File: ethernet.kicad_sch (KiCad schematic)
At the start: 17 parts, among them J3 HR911130C, U1 AM6254ATCGHAALW, U6 RTL8211F-CG

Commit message: Ethernet chip wiring
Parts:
- added R65: RC0402FR-072K49L, pepy_sym_lib:[RES_SMD_0402_1005Metric], symbol pepy_sym_lib:[RES_SMD_0402_1005Metric]YAGEO RC0402FR-072K49L
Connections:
- net GND: now also R65.2
- net at U6.39 (RSET): now also R65.1
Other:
- note added: "Place resistors close to IC"
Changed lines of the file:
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@@
 	(generator_version "9.0")
 	(paper "A3")
+	(text "Place resistors close to IC\n"
+		(exclude_from_sim no)
+		(at 133.096 259.588 0)
+		(effects
+			(font
+				(size 1.27 1.27)
+			)
+		)
+	)
 	(text "2kV Cap\n"
 		(exclude_from_sim no)
@@
 	)
 	(symbol
+		(lib_id "power:GND")
+		(at 120.65 85.09 90)
+		(unit 1)
+		(exclude_from_sim no)
+		(in_bom yes)
+		(on_board yes)
+		(dnp no)
+		(property "Reference" "#PWR037"
+			(at 127 85.09 0)
+			(effects
+				(font
+					(size 1.27 1.27)
+				)
+				(hide yes)
+			)
+		)
+		(property "Value" "GND"
+			(at 123.698 85.09 90)
+			(effects
+				(font
+					(size 1.27 1.27)
+				)
+				(justify right)
+			)
+		)
+		(property "Footprint" ""
+			(at 120.65 85.09 0)
+			(effects
+				(font
+					(size 1.27 1.27)
+				)
+				(hide yes)
+			)
+		)
+		(property "Datasheet" ""
+			(at 120.65 85.09 0)
+			(effects
+				(font
+					(size 1.27 1.27)
+				)
+				(hide yes)
+			)
+		)
+		(property "Description" "Power symbol creates a global label with name \"GND\" , ground"
+			(at 120.65 85.09 0)
+			(effects
+				(font
+					(size 1.27 1.27)
+				)
+				(hide yes)
+			)
+		)
+		(pin "1"
+		)
+		(instances
+			(project ""
+				(path "/30d6913c-7aa4-4f56-9882-2ba08f7e2cce/0115f286-8e80-4bc6-a636-ca28db07176d"
+					(reference "#PWR037")
+					(unit 1)
+				)
+			)
+		)
+	)
+	(symbol
 		(lib_id "pepy_sym_lib:[RES_SMD_0201_0603Metric]YAGEO RC0201FR-0733RL")
 		(at 93.98 242.57 0)
@@
 					(unit 1)
 				)
+			)
+		)
+	)
+	(symbol
+		(lib_id "pepy_sym_lib:[RES_SMD_0402_1005Metric]YAGEO RC0402FR-072K49L")
+		(at 115.57 85.09 0)
+		(unit 1)
+		(exclude_from_sim no)
+		(in_bom yes)
+		(on_board yes)
+		(dnp no)
+		(property "Reference" "R65"
+			(at 115.57 81.28 0)
+			(effects
+				(font
+					(size 1.27 1.27)
+				)
+			)
+		)
+		(property "Value" "RC0402FR-072K49L"
+			(at 115.57 90.17 0)
+			(effects
+				(font
+					(size 1.27 1.27)
+				)
+				(hide yes)
+			)
+		)
+		(property "Footprint" "pepy_sym_lib:[RES_SMD_0402_1005Metric]"
+			(at 115.57 92.71 0)
+			(effects
+				(font
+					(size 1.27 1.27)
+				)
+				(hide yes)
+			)
+		)
+		(property "Datasheet" "https://www.lcsc.com/product-detail/Chip-Resistor-Surface-Mount_YAGEO-RC0402FR-072K49L_C145071.html"
+			(at 115.57 95.25 0)
+			(effects
+				(font
+					(size 1.27 1.27)
+				)
+				(hide yes)
+			)
+		)
+		(property "Description" "1/16W Thick Film Resistors 50V ±100ppm/℃ ±1% 2.49kΩ 0402 Chip Resistor - Surface Mount ROHS"
+			(at 115.062 100.33 0)
+			(effects
+				(font
+					(size 1.27 1.27)
+				)
+				(hide yes)
+			)
+		)
+		(property "LCSC Part" "C145071"
+			(at 115.57 97.79 0)
+			(effects
+				(font
+					(size 1.27 1.27)
+				)
+				(hide yes)
+			)
+		)
+		(property "Nvalue" "2.49k"
+			(at 115.57 83.058 0)
+			(effects
+				(font
+					(size 1.27 1.27)
+				)
+			)
+		)
+		(property "Manufacturer" "YAGEO"
+			(at 114.554 102.616 0)
+			(effects
+				(font
+					(size 1.27 1.27)
+				)
+				(hide yes)
+			)
+		)
+		(property "Package" "0402"
+			(at 115.316 104.648 0)
+			(effects
+				(font
+					(size 1.27 1.27)
+				)
+				(hide yes)
+			)
+		)
+		(pin "2"
+		)
+		(pin "1"
+		)
+		(instances
+			(project ""
+				(path "/30d6913c-7aa4-4f56-9882-2ba08f7e2cce/0115f286-8e80-4bc6-a636-ca28db07176d"
+					(reference "R65")
+					(unit 1)
+				)

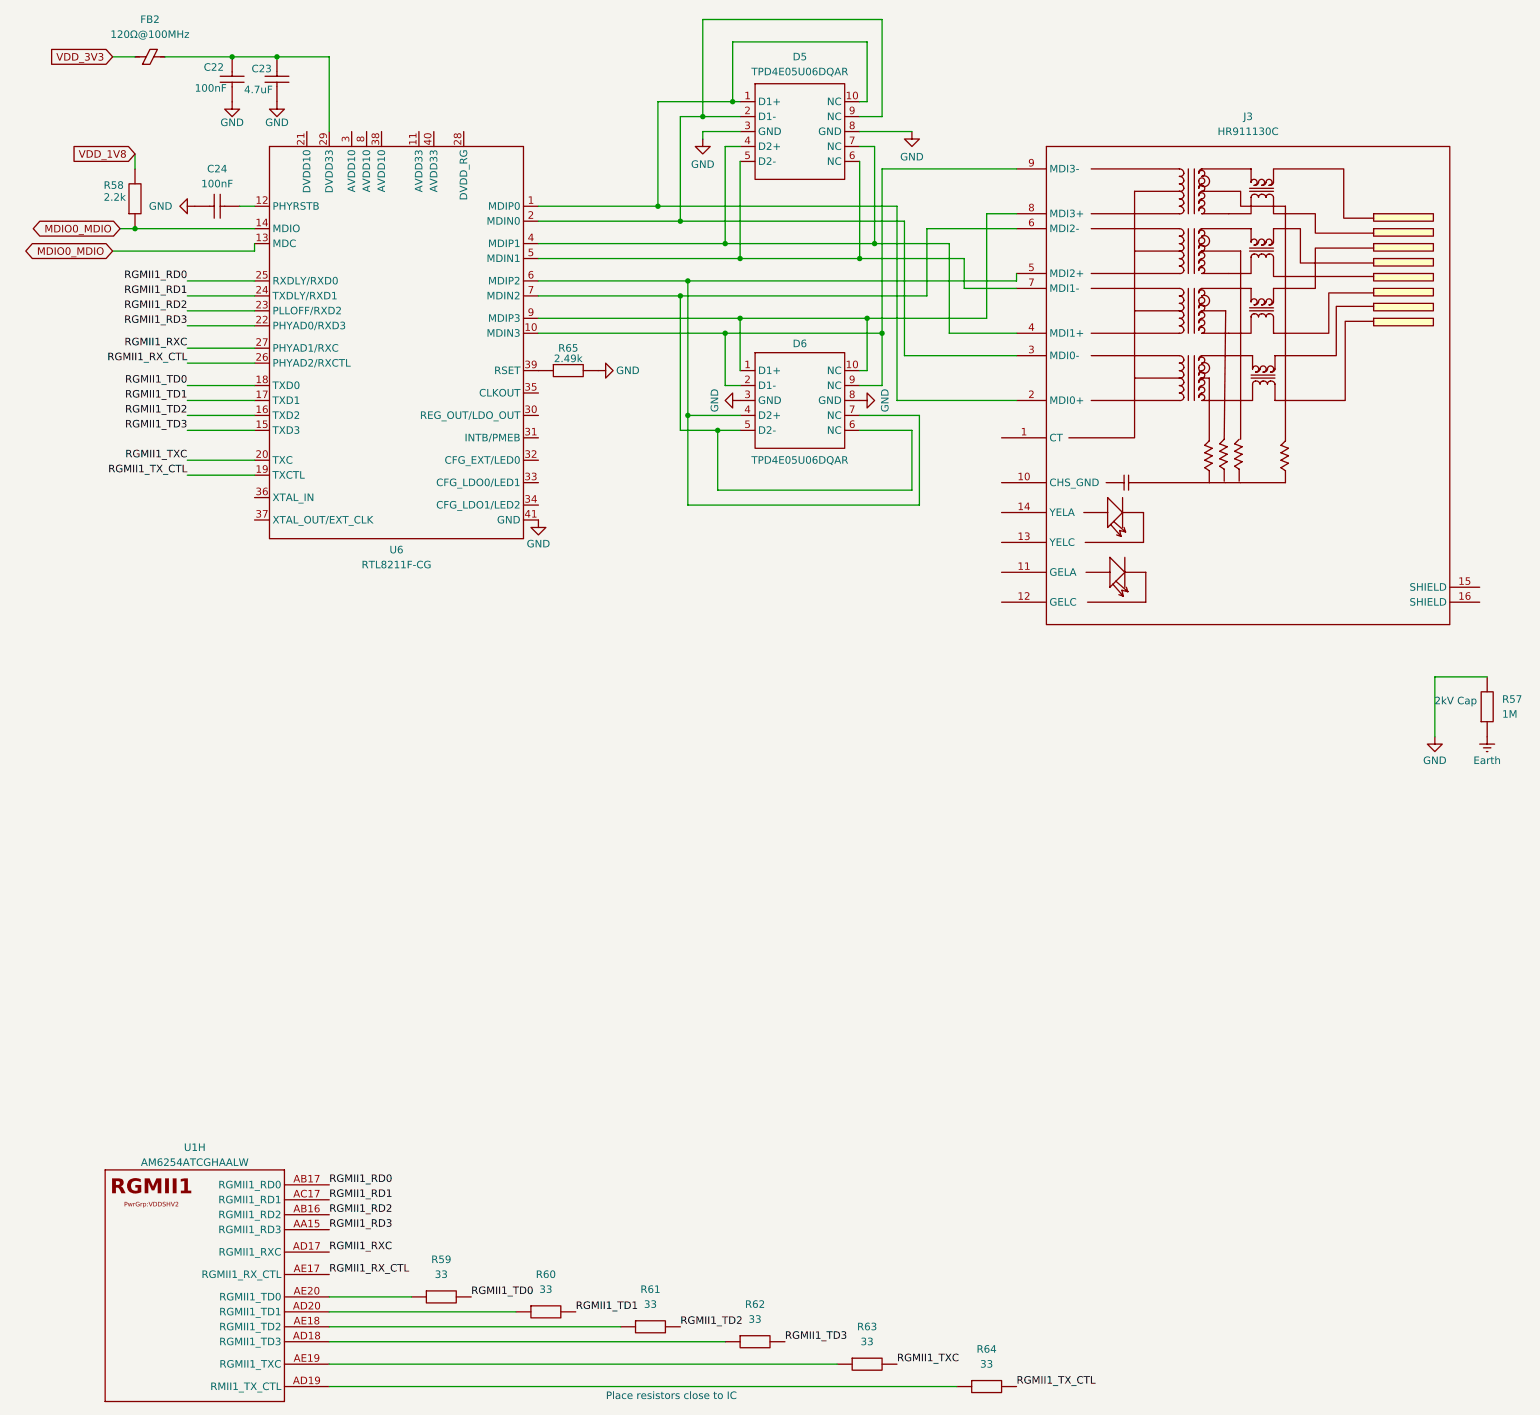
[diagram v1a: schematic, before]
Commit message: SD card changes
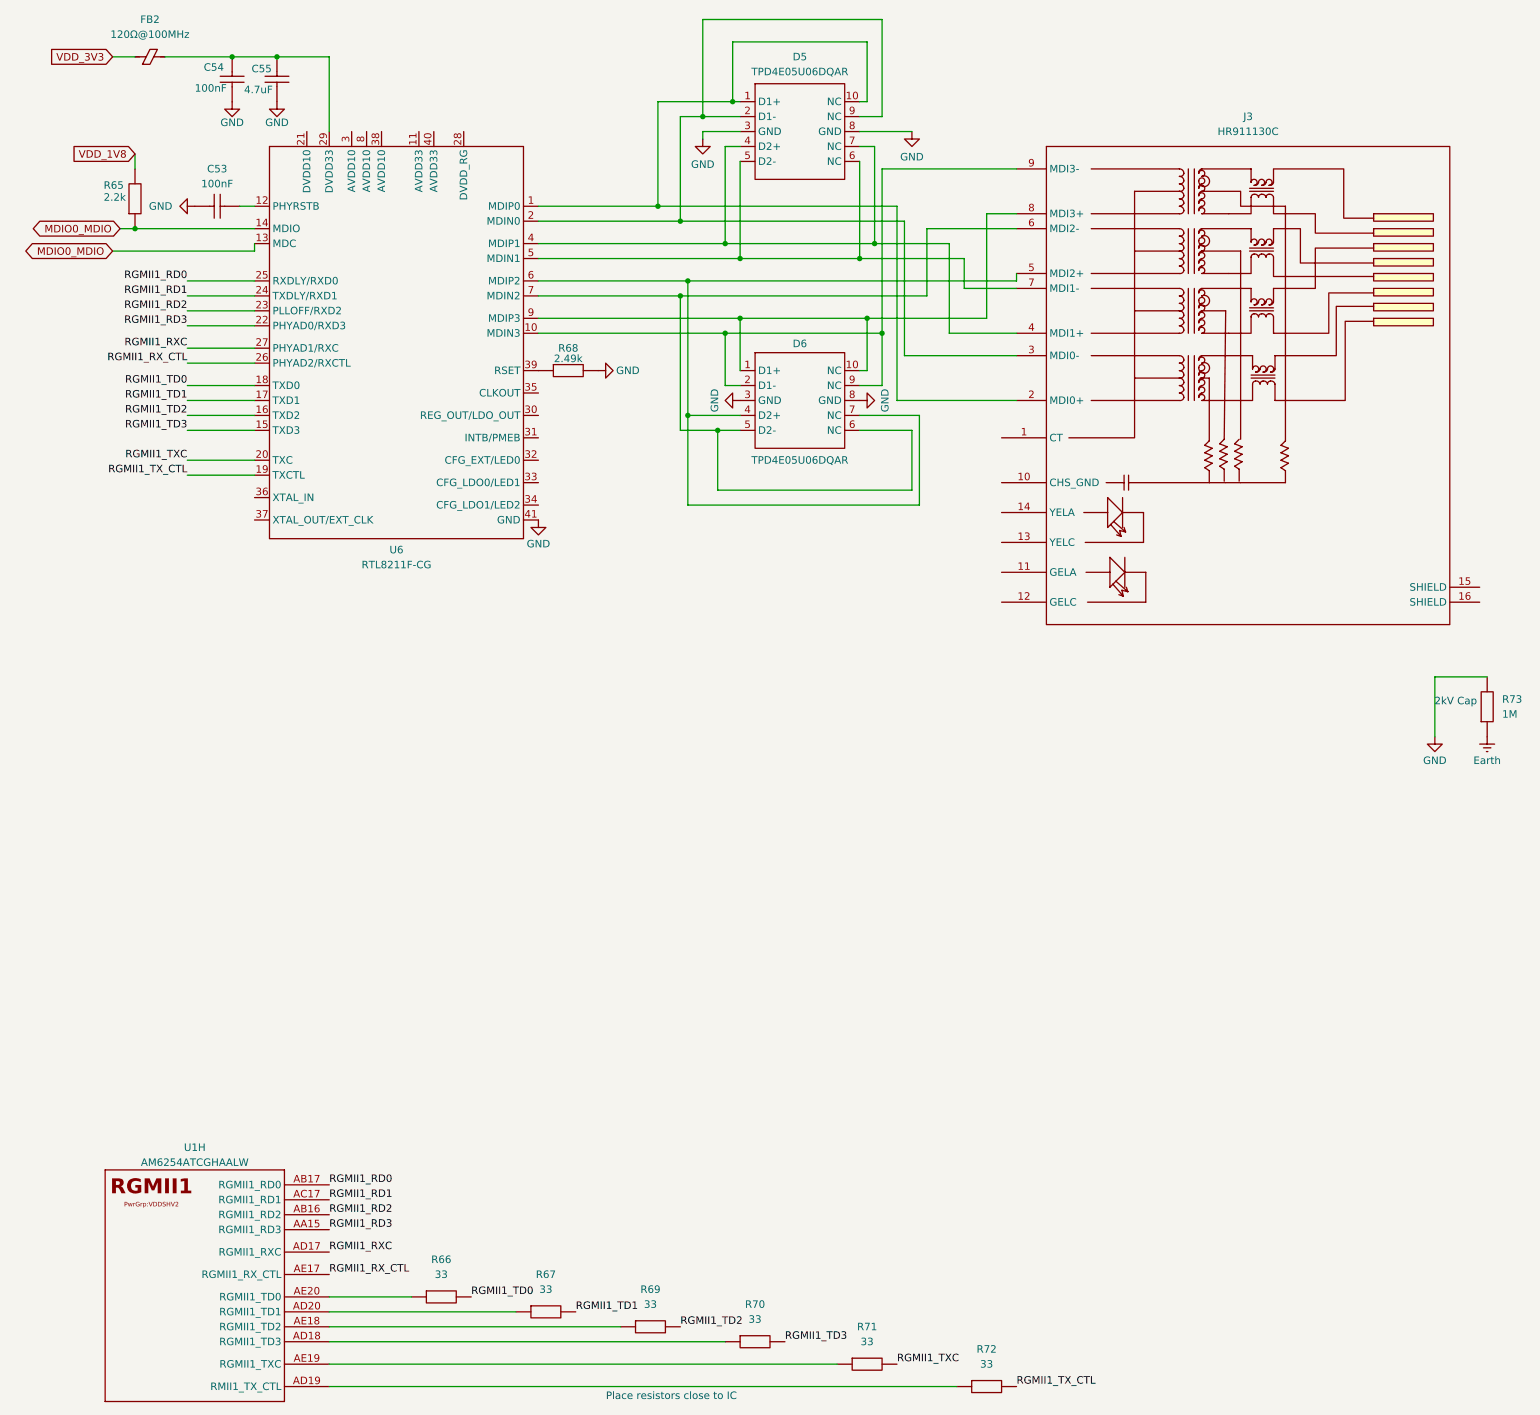
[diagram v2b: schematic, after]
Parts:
- renumbered C24 to C53, C22 to C54, C23 to C55, R58 to R65, R59 to R66, R60 to R67, R65 to R68, R61 to R69, R62 to R70, R63 to R71, R64 to R72, R57 to R73
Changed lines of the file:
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@@
 		(on_board yes)
 		(dnp no)
-		(property "Reference" "#PWR035"
+		(property "Reference" "#PWR050"
 			(at 171.45 90.17 0)
 			(effects
@@
 			(project "dashcam"
 				(path "/30d6913c-7aa4-4f56-9882-2ba08f7e2cce/0115f286-8e80-4bc6-a636-ca28db07176d"
-					(reference "#PWR035")
+					(reference "#PWR050")
 					(unit 1)
 				)
@@
 		(on_board yes)
 		(dnp no)
-		(property "Reference" "#PWR030"
+		(property "Reference" "#PWR053"
 			(at 271.78 153.67 0)
 			(effects
@@
 			(project ""
 				(path "/30d6913c-7aa4-4f56-9882-2ba08f7e2cce/0115f286-8e80-4bc6-a636-ca28db07176d"
-					(reference "#PWR030")
+					(reference "#PWR053")
 					(unit 1)
 				)
@@
 		(dnp no)
 		(fields_autoplaced yes)
-		(property "Reference" "R61"
+		(property "Reference" "R69"
 			(at 129.54 241.3 0)
 			(effects
@@
 			(project "dashcam"
 				(path "/30d6913c-7aa4-4f56-9882-2ba08f7e2cce/0115f286-8e80-4bc6-a636-ca28db07176d"
-					(reference "R61")
+					(reference "R69")
 					(unit 1)
 				)
@@
 		(dnp no)
 		(fields_autoplaced yes)
-		(property "Reference" "#PWR036"
+		(property "Reference" "#PWR043"
 			(at 45.72 57.15 0)
 			(effects
@@
 			(project ""
 				(path "/30d6913c-7aa4-4f56-9882-2ba08f7e2cce/0115f286-8e80-4bc6-a636-ca28db07176d"
-					(reference "#PWR036")
+					(reference "#PWR043")
 					(unit 1)
 				)
@@
 		(on_board yes)
 		(dnp no)
-		(property "Reference" "#PWR028"
+		(property "Reference" "#PWR044"
 			(at 58.42 45.72 0)
 			(effects
@@
 			(project ""
 				(path "/30d6913c-7aa4-4f56-9882-2ba08f7e2cce/0115f286-8e80-4bc6-a636-ca28db07176d"
-					(reference "#PWR028")
+					(reference "#PWR044")
 					(unit 1)
 				)
@@
 		(on_board yes)
 		(dnp no)
-		(property "Reference" "#PWR031"
+		(property "Reference" "#PWR052"
 			(at 262.89 153.67 0)
 			(effects
@@
 			(project ""
 				(path "/30d6913c-7aa4-4f56-9882-2ba08f7e2cce/0115f286-8e80-4bc6-a636-ca28db07176d"
-					(reference "#PWR031")
+					(reference "#PWR052")
 					(unit 1)
 				)
@@
 		(on_board yes)
 		(dnp no)
-		(property "Reference" "#PWR034"
+		(property "Reference" "#PWR049"
 			(at 138.43 90.17 0)
 			(effects
@@
 			(project "dashcam"
 				(path "/30d6913c-7aa4-4f56-9882-2ba08f7e2cce/0115f286-8e80-4bc6-a636-ca28db07176d"
-					(reference "#PWR034")
+					(reference "#PWR049")
 					(unit 1)
 				)
@@
 		(dnp no)
 		(fields_autoplaced yes)
-		(property "Reference" "R62"
+		(property "Reference" "R70"
 			(at 147.32 243.84 0)
 			(effects
@@
 			(project "dashcam"
 				(path "/30d6913c-7aa4-4f56-9882-2ba08f7e2cce/0115f286-8e80-4bc6-a636-ca28db07176d"
-					(reference "R62")
+					(reference "R70")
 					(unit 1)
 				)
@@
 		(on_board yes)
 		(dnp no)
-		(property "Reference" "#PWR027"
+		(property "Reference" "#PWR046"
 			(at 110.49 116.84 0)
 			(effects
@@
 			(project ""
 				(path "/30d6913c-7aa4-4f56-9882-2ba08f7e2cce/0115f286-8e80-4bc6-a636-ca28db07176d"
-					(reference "#PWR027")
+					(reference "#PWR046")
 					(unit 1)
 				)
@@
 		(on_board yes)
 		(dnp no)
-		(property "Reference" "#PWR029"
+		(property "Reference" "#PWR045"
 			(at 66.04 45.72 0)
 			(effects
@@
 			(project "dashcam"
 				(path "/30d6913c-7aa4-4f56-9882-2ba08f7e2cce/0115f286-8e80-4bc6-a636-ca28db07176d"
-					(reference "#PWR029")
+					(reference "#PWR045")
 					(unit 1)
 				)
@@
 		(on_board yes)
 		(dnp no)
-		(property "Reference" "#PWR037"
+		(property "Reference" "#PWR047"
 			(at 127 85.09 0)
 			(effects
@@
 			(project ""
 				(path "/30d6913c-7aa4-4f56-9882-2ba08f7e2cce/0115f286-8e80-4bc6-a636-ca28db07176d"
-					(reference "#PWR037")
+					(reference "#PWR047")
 					(unit 1)
 				)
@@
 		(dnp no)
 		(fields_autoplaced yes)
-		(property "Reference" "R59"
+		(property "Reference" "R66"
 			(at 93.98 236.22 0)
 			(effects
@@
 			(project ""
 				(path "/30d6913c-7aa4-4f56-9882-2ba08f7e2cce/0115f286-8e80-4bc6-a636-ca28db07176d"
-					(reference "R59")
+					(reference "R66")
 					(unit 1)
 				)
@@
 		(on_board yes)
 		(dnp no)
-		(property "Reference" "#PWR033"
+		(property "Reference" "#PWR048"
 			(at 138.43 52.07 0)
 			(effects
@@
 			(project "dashcam"
 				(path "/30d6913c-7aa4-4f56-9882-2ba08f7e2cce/0115f286-8e80-4bc6-a636-ca28db07176d"
-					(reference "#PWR033")
+					(reference "#PWR048")
 					(unit 1)
 				)
@@
 		(on_board yes)
 		(dnp no)
-		(property "Reference" "R58"
+		(property "Reference" "R65"
 			(at 36.576 53.594 90)
 			(effects
@@
 			(project ""
 				(path "/30d6913c-7aa4-4f56-9882-2ba08f7e2cce/0115f286-8e80-4bc6-a636-ca28db07176d"
-					(reference "R58")
+					(reference "R65")
 					(unit 1)
 				)
@@
 		(dnp no)
 		(fields_autoplaced yes)
-		(property "Reference" "R63"
+		(property "Reference" "R71"
 			(at 166.37 247.65 0)
 			(effects
@@
 			(project "dashcam"
 				(path "/30d6913c-7aa4-4f56-9882-2ba08f7e2cce/0115f286-8e80-4bc6-a636-ca28db07176d"
-					(reference "R63")
+					(reference "R71")
 					(unit 1)
 				)
@@
 		(on_board yes)
 		(dnp no)
-		(property "Reference" "C23"
+		(property "Reference" "C55"
 			(at 61.722 33.782 90)
 			(effects
@@
 			(project ""
 				(path "/30d6913c-7aa4-4f56-9882-2ba08f7e2cce/0115f286-8e80-4bc6-a636-ca28db07176d"
-					(reference "C23")
+					(reference "C55")
 					(unit 1)
 				)
@@
 		(dnp no)
 		(fields_autoplaced yes)
-		(property "Reference" "R64"
+		(property "Reference" "R72"
 			(at 186.69 251.46 0)
 			(effects
@@
 			(project "dashcam"
 				(path "/30d6913c-7aa4-4f56-9882-2ba08f7e2cce/0115f286-8e80-4bc6-a636-ca28db07176d"
-					(reference "R64")
+					(reference "R72")
 					(unit 1)
 				)
@@
 		(dnp no)
 		(fields_autoplaced yes)
-		(property "Reference" "R60"
+		(property "Reference" "R67"
 			(at 111.76 238.76 0)
 			(effects
@@
 			(project "dashcam"
 				(path "/30d6913c-7aa4-4f56-9882-2ba08f7e2cce/0115f286-8e80-4bc6-a636-ca28db07176d"
-					(reference "R60")
+					(reference "R67")
 					(unit 1)
 				)
@@
 		(dnp no)
 		(fields_autoplaced yes)
-		(property "Reference" "C24"
+		(property "Reference" "C53"
 			(at 55.88 50.8 0)
 			(effects
@@
 			(project ""
 				(path "/30d6913c-7aa4-4f56-9882-2ba08f7e2cce/0115f286-8e80-4bc6-a636-ca28db07176d"
-					(reference "C24")
+					(reference "C53")
 					(unit 1)
 				)
@@
 		(on_board yes)
 		(dnp no)
-		(property "Reference" "R65"
+		(property "Reference" "R68"
 			(at 115.57 81.28 0)
 			(effects
@@
 			(project ""
 				(path "/30d6913c-7aa4-4f56-9882-2ba08f7e2cce/0115f286-8e80-4bc6-a636-ca28db07176d"
-					(reference "R65")
+					(reference "R68")
 					(unit 1)
 				)
@@
 		(on_board yes)
 		(dnp no)
-		(property "Reference" "C22"
+		(property "Reference" "C54"
 			(at 53.594 33.528 90)
 			(effects
@@
 			(project ""
 				(path "/30d6913c-7aa4-4f56-9882-2ba08f7e2cce/0115f286-8e80-4bc6-a636-ca28db07176d"
-					(reference "C22")
+					(reference "C54")
 					(unit 1)
 				)
@@
 		(on_board yes)
 		(dnp no)
-		(property "Reference" "#PWR032"
+		(property "Reference" "#PWR051"
 			(at 173.99 50.8 0)
 			(effects
@@
 			(project ""
 				(path "/30d6913c-7aa4-4f56-9882-2ba08f7e2cce/0115f286-8e80-4bc6-a636-ca28db07176d"
-					(reference "#PWR032")
+					(reference "#PWR051")
 					(unit 1)
 				)
@@
 		(dnp no)
 		(fields_autoplaced yes)
-		(property "Reference" "R57"
+		(property "Reference" "R73"
 			(at 274.32 140.9699 90)
 			(effects
@@
 			(project ""
 				(path "/30d6913c-7aa4-4f56-9882-2ba08f7e2cce/0115f286-8e80-4bc6-a636-ca28db07176d"
-					(reference "R57")
+					(reference "R73")
 					(unit 1)
 				)
